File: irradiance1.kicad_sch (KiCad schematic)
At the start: 30 parts, among them IC1 TSL25911FN, J2 Battery, J3 CAN_In, J4 CAN_Out, U1 ADM3055E, U2 Nucleo_L432KC, U3 CDSOT23-T24CAN

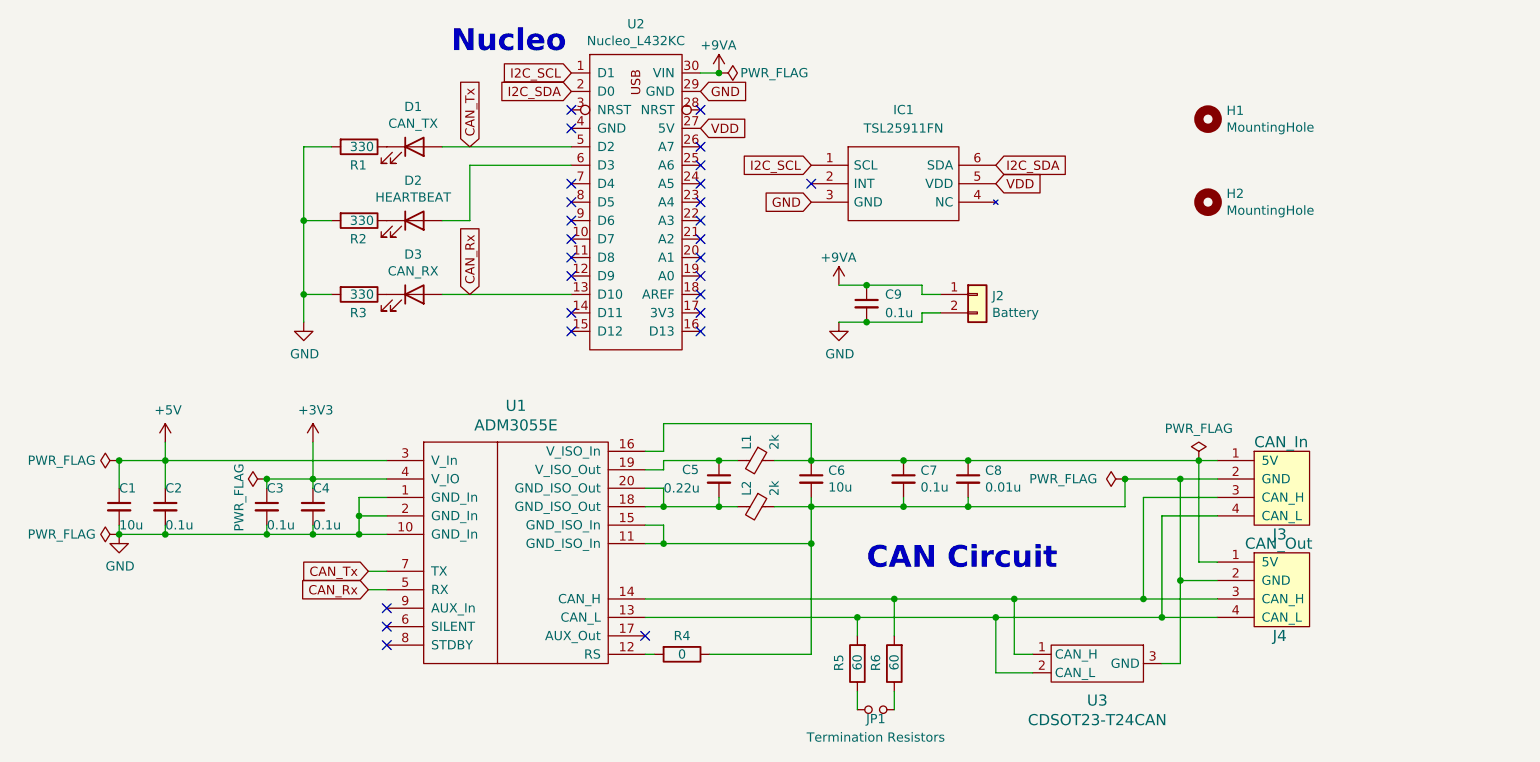
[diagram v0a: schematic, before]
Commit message: Made updates based on feedback: - Added series schottky diode for reverse polarity protection at J2 - Added cap and open-drain resistors for light sensor (IC1) - Connected grounds on Nucleo - Added 10 uF cap at J2 - Other small changes
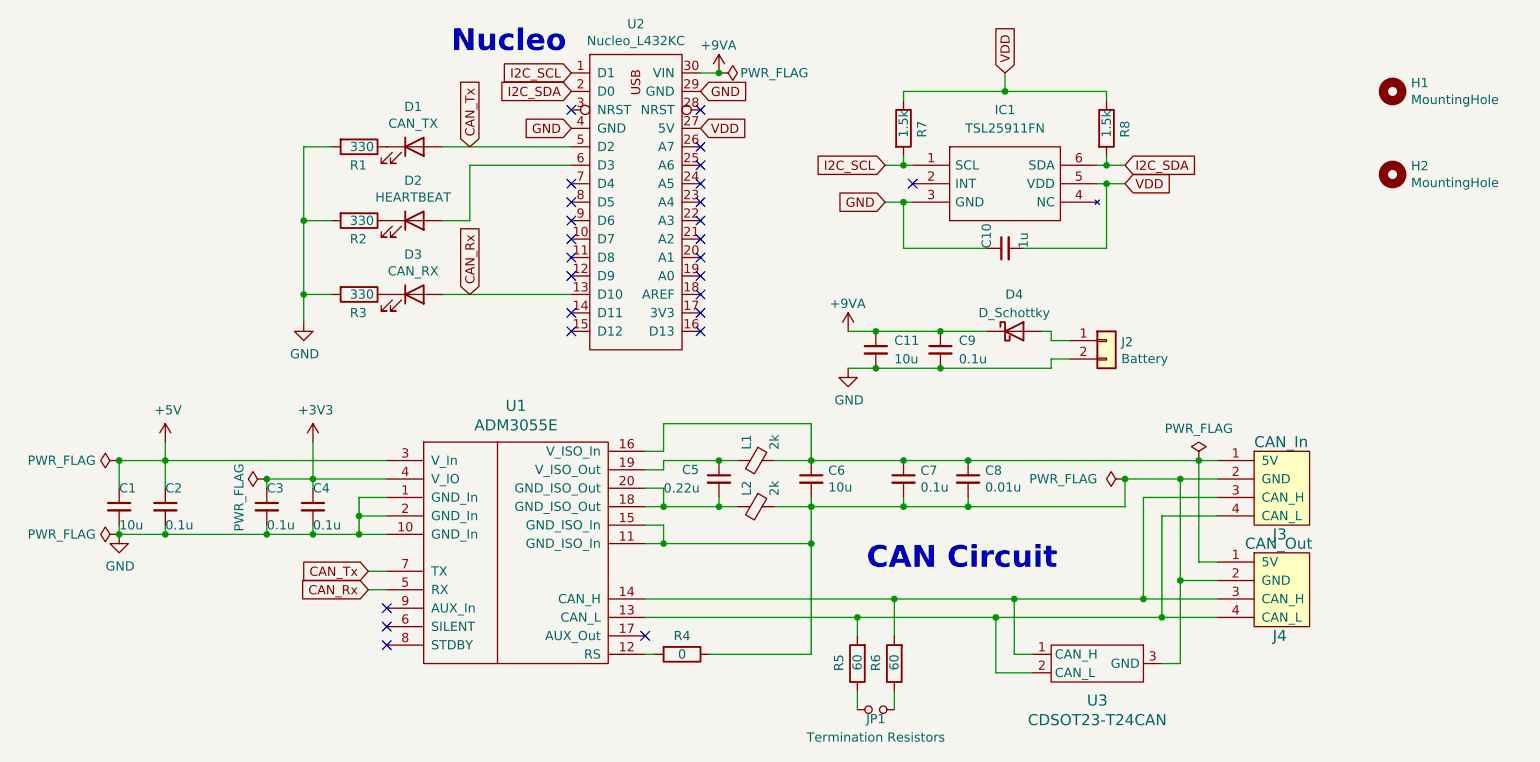
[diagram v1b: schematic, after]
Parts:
- added C10: 1u, Capacitor_SMD:C_0402_1005Metric_Pad0.74x0.62mm_HandSolder, symbol Device:C_Small
- added C11: 10u, Capacitor_SMD:C_0402_1005Metric_Pad0.74x0.62mm_HandSolder, symbol Device:C_Small
- added D4: D_Schottky, irradianceboard:SODFL5436X110N, symbol Device:D_Schottky
- added R7, R8: 1.5k, Resistor_SMD:R_0402_1005Metric_Pad0.72x0.64mm_HandSolder, symbol irradiance1-rescue:R-MPPT-rescue
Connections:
- net +9VA: now also C11.1, D4.1 (K); no longer J2.1 (Pin_1)
- net GND: now also U2.4 (GND), C10.1, C11.2
- net I2C_SCL: now also R7.2
- net I2C_SDA: now also R8.2
- net VDD: now also C10.2, R7.1, R8.1
- new net: D4.2 (A), J2.1 (Pin_1)
- no-connect marks 27 -> 26
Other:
- moved on the sheet: C9, H1, H2, IC1, J2
